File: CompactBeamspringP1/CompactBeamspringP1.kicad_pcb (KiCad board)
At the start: 2 copper layers, 162.3 x 23.5 mm, 29 parts, among them J1 BEAMSPRING CONNECTOR, J3 EXPANSION HEADER, U1 MCP4921-E, U2 LM339A, U3 74AHC595, U4 74AHC595, U5 ProMicro, U7 74AHC595

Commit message: More mods
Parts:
- added J2: PadsToShort, TH-XWhatsIt:PadsToShort, B.Cu at (113.7, 112.1)
- added R8: Not Mounted, Resistor_SMD:R_0805_2012Metric_Pad1.15x1.40mm_HandSolder, B.Cu at (137.1, 116.6)
- added TP1: Dac Output, TestPoint:TestPoint_Pad_D1.0mm, B.Cu at (245.7, 124.7)
- added TP2: Threshold Voltage, TestPoint:TestPoint_Pad_D1.0mm, B.Cu at (261.5, 123.5)
- R6: value Not Mounted, Shorted -> Not Mounted; footprint TH-XWhatsIt:SHORTEDR_0805_2012Metric_Pad1.15x1.40mm_HandSolder -> Resistor_SMD:R_0805_2012Metric_Pad1.15x1.40mm_HandSolder
- moved R6 0.85 mm to (137.1, 112.6)
- moved R7 0.83 mm to (137.1, 114.6)
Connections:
- net Net-(NT1-Pad2) renamed GND
- U5 pad 1: HEADER1 -> HEADER3
- U5 pad 10: ROW6 -> HEADER2
- U5 pad 11: ROW3 -> Net-(U5-Pad11)
- U5 pad 12: ROW1 -> Net-(U5-Pad12)
- U5 pad 15: GNDD -> Net-(R8-Pad1)
- U5 pad 19: HEADER3 -> Net-(U5-Pad19)
- U5 pad 2: HEADER2 -> HEADER4
- U5 pad 20: HEADER4 -> Net-(U5-Pad20)
- U5 pad 5: ROW8 -> ROW2
- U5 pad 6: ROW7 -> ROW1
- U5 pad 7: ROW2 -> ROW4
- U5 pad 8: ROW5 -> ROW3
- U5 pad 9: ROW4 -> HEADER1
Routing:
- net HEADER3: track 20.6 -> 45.0 mm
- net GNDD: track 134.0 -> 110.9 mm, vias 63 -> 73
- net GNDA: track 152.6 -> 131.3 mm, vias 26 -> 32
- net HEADER4: track 25.7 -> 43.6 mm
- net Net-(R8-Pad1): track 0.00 -> 15.1 mm
- net ROW1: track 119.6 -> 132.8 mm
- net HEADER2: track 45.2 -> 33.4 mm, vias 0 -> 2
- net +5VD: track 148.1 -> 158.6 mm
- net HEADER1: track 54.2 -> 43.9 mm, vias 0 -> 2
- net +5VA: track 186.8 -> 196.9 mm, vias 0 -> 2
- net ROW3: track 118.2 -> 127.8 mm
- net RST: track 0.00 -> 6.35 mm
- net Net-(R4-Pad2): track 2.66 -> 8.98 mm
- net SETPOINT: track 28.3 -> 33.5 mm
- net ROW2: track 131.8 -> 136.9 mm
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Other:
- board text added: "Compact-Beamspring Rev1.2"
- board text added: "DAC"
- board text added: "Threshold"
- board text added: "Voltage"
- board text added: "Vout"
- board text removed: "Compact-Beamspring Rev1.1"

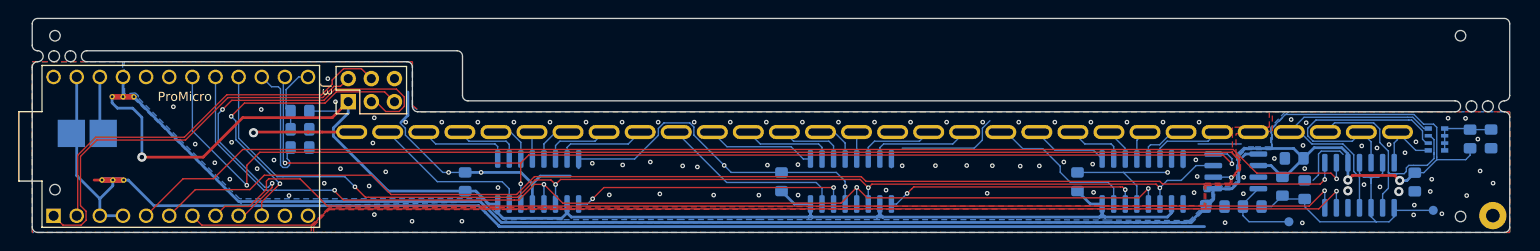
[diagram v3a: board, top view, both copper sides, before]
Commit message: Moved to individual resistors instead of resistor network, added a bit more space next to the promicro
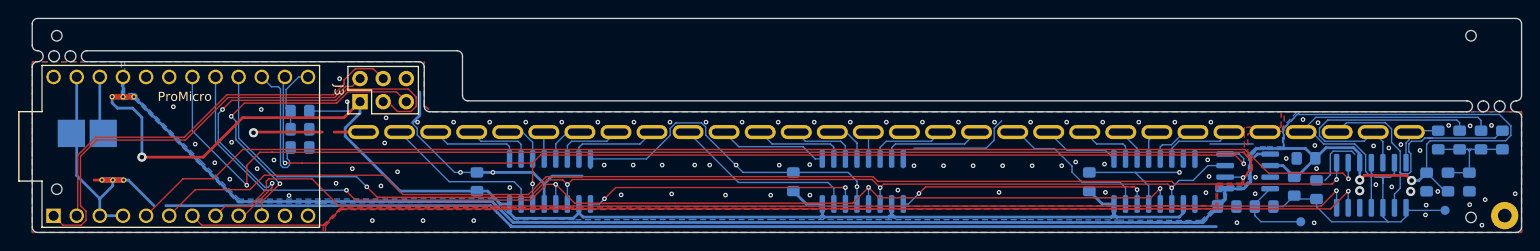
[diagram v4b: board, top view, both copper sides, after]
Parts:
- removed the REF** at (110.2, 121.2)
- removed the REF** at (264.5, 124.2)
- removed RN1: 100K, Resistor_SMD:R_Array_Convex_4x0603
- added R10: 100k 1%, Resistor_SMD:R_0805_2012Metric_Pad1.15x1.40mm_HandSolder, B.Cu at (262.1, 115.8)
- added R11: 100k 1%, Resistor_SMD:R_0805_2012Metric_Pad1.15x1.40mm_HandSolder, B.Cu at (266.8, 115.8)
- added R12: 100k 1%, Resistor_SMD:R_0805_2012Metric_Pad1.15x1.40mm_HandSolder, B.Cu at (269.1, 115.8)
- added R9: 100k 1%, Resistor_SMD:R_0805_2012Metric_Pad1.15x1.40mm_HandSolder, B.Cu at (264.4, 115.8)
- added REF**: tooling_hole, TH-XWhatsIt:tooling_hole, F.Cu at (110.3, 121.2)
- added REF**: tooling_hole, TH-XWhatsIt:tooling_hole, F.Cu at (265.6, 124.2)
- moved R1 5.31 mm to (263.1, 120.4)
- moved R2 5.30 mm to (265.5, 120.4)
- moved C1 1.30 mm to (238.9, 123.1)
- moved C2 1.30 mm to (156.5, 120.3)
- moved C3 1.30 mm to (260.8, 120.4)
- moved C5 1.30 mm to (223.7, 120.3)
- moved C6 1.30 mm to (247.5, 117.8)
- moved H1 1.30 mm to (269.4, 124.0)
- moved J1 1.30 mm to (201.5, 114.9)
- moved R4 1.30 mm to (242.9, 123.1)
- moved R5 1.30 mm to (248.7, 121.2)
- moved TP2 1.30 mm to (262.8, 123.5)
- moved U2 1.30 mm to (254.7, 120.7)
- moved U4 1.30 mm to (198.9, 120.3)
- moved U7 1.30 mm to (230.9, 120.3)
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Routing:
- net +5VA: track 196.9 -> 210.6 mm
- net SENSE3: track 26.0 -> 32.1 mm
- net SENSE4: track 30.6 -> 35.9 mm
- net BIAS: track 7.55 -> 12.5 mm
- net +5VD: track 158.6 -> 161.2 mm
- net SENSE2: track 26.4 -> 28.0 mm
- net ~SELECTDAC: track 130.8 -> 132.2 mm
- net MOSI: track 122.7 -> 124.0 mm
- net CLOCK: track 125.2 -> 126.5 mm
- net ROW1: track 132.8 -> 134.1 mm
- net ROW4: track 129.4 -> 130.7 mm
- net ROW3: track 127.8 -> 129.1 mm
- net ROW2: track 136.9 -> 138.2 mm
- net LOADCOL: track 121.2 -> 122.5 mm
- net HEADER4: track 43.6 -> 44.9 mm
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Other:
- board size 162.3 x 23.5 mm -> 163.6 x 23.5 mm
- board text added: "Compact-Beamspring Rev1.3"
- board text removed: "Compact-Beamspring Rev1.2"
